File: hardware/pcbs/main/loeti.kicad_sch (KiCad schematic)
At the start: 104 parts, among them J1 REDFIT_SWD_6, J2 DATA, J3 POWER, J5 Conn_01x05_Pin, Q1 Si4162DY, Q2 BC817, Q4 BC817, Q5 BC807, Q6 Si4425FDY, SW1 BOOT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

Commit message: feat: improve code structure, EEPROM with checksum
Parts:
- Q6: value Si4425FDY -> Si4825
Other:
- note added: "Possible candidates Si4825DDY Si4425DDY DMP3036SSS"
- note removed: "Possible candidates Si4425FDY (best) Si4425DDY Si4825DDY DMG4435SSS IRF9393PbF"
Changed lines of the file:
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@@
 		)
 	)
-	(text "Possible candidates\nSi4425FDY (best)\nSi4425DDY\nSi4825DDY\nDMG4435SSS\nIRF9393PbF"
+	(text "Possible candidates\nSi4825DDY\nSi4425DDY\nDMP3036SSS"
 		(exclude_from_sim no)
 		(at 390.144 154.94 0)
@@
 		)
 	)
+	(polyline
+		(pts
+			(xy 402.59 196.85) (xy 403.86 196.85)
+		)
+		(stroke
+			(width 0)
+			(type solid)
+		)
+	)
 	(wire
 		(pts
@@
 		(on_board yes)
 		(dnp no)
-		(fields_autoplaced yes)
 		(property "Reference" "#FLG08"
 			(at 102.235 207.01 0)
@@
 			)
 		)
-		(property "Value" "Si4425FDY"
+		(property "Value" "Si4825"
 			(at 368.3 173.9899 0)
 			(effects

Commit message: fix: pmos type
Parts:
- Q6: value Si4825 -> Si4425FDY
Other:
- note added: "Possible candidates Si4151DY Si4153DY Si4825DDY"
- note removed: "Possible candidates Si4825DDY Si4425DDY DMP3036SSS"
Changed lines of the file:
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@@
 		)
 	)
-	(text "Possible candidates\nSi4825DDY\nSi4425DDY\nDMP3036SSS"
+	(text "Possible candidates\nSi4151DY\nSi4153DY\nSi4825DDY"
 		(exclude_from_sim no)
 		(at 390.144 154.94 0)
@@
 			)
 		)
-		(property "Value" "Si4825"
+		(property "Value" "Si4425FDY"
 			(at 368.3 173.9899 0)
 			(effects

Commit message: feat: v7a initial hardware design
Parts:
- removed C30: ~, Capacitor_SMD:C_0603_1608Metric, symbol Device:C
- removed U11: TLV333DBV, Package_TO_SOT_SMD:SOT-23-5, symbol Amplifier_Operational:TLV2371DBV
- added C2: 100n, Capacitor_SMD:C_0603_1608Metric, symbol Device:C
- added D10: BAT54S, Package_TO_SOT_SMD:SOT-23, symbol Diode:BAT54S
- added R29, R37: 220k, Resistor_SMD:R_0603_1608Metric, symbol Device:R
- added R38: 1k, Resistor_SMD:R_0603_1608Metric, symbol Device:R
- added U7: TLV2333, Package_SO:SOIC-8_3.9x4.9mm_P1.27mm, symbol Amplifier_Operational:TLV2372
- C29: value 330p -> 22p; MPN C1664 -> C1653
- Q6: value Si4425FDY -> Si4825
- R23: value 1M -> 22k; MPN C22935 -> C31850
- R24: value 10k -> 22k; MPN C25804 -> C31850
- R26: value 1k -> 10k; MPN C21190 -> C25804
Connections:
- net +3V3: now also D10.2 (K), U7.8 (V+); no longer R23.1
- net ADC1_IN1: now also D2.3 (COM), R10.2; no longer C29.1, R25.1
- net ADC1_IN2: now also C29.1, R25.2, D10.3 (COM), U7.7; no longer D2.3 (COM), R10.2
- net GND: now also C2.2, D10.1 (A), R29.1, U7.4 (V-)
- net SLP_EXT: now also J5.1 (Pin_1); no longer J5.3 (Pin_3)
- net at C29.2, R26.1: now also R25.1, U7.6 (-); no longer R25.2
- net at R24.2: now also R37.1, U7.2 (-)
- net HEATER renamed RED
- net RED: now also R23.2
- removed net TC+: J5.1 (Pin_1), R23.2, R24.1
- new net: C2.1, R38.2, U7.5 (+)
- new net: R23.1, R29.2, U7.3 (+)
- new net: R37.2, R38.1, U7.1
- new net GREEN: J5.3 (Pin_3), R24.1
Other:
- note added: "Feedback: ~33 kHz low-pass"
- note added: "Gain 10"
- note added: "Gain 23"
- note added: "Possible candidates Si4825DDY Si4425DDY DMP3036SSS"
- note added: "Thermocouple amplifier - gain 230"
- note added: "~1.6 kHz low-pass"
- note removed: "C210 1_COM: green+blue 2_TC+: red 3_HEATER: red"
- note removed: "C245 1_COM: green 2_TC+: red 3_HEATER: blue"
- note removed: "Feedback: 2180 Hz low-pass"
- note removed: "Possible candidates Si4151DY Si4153DY Si4825DDY"
- note removed: "Thermocouple amplifier"
- moved on the sheet: D2, J5, R10, R24, R25, R9

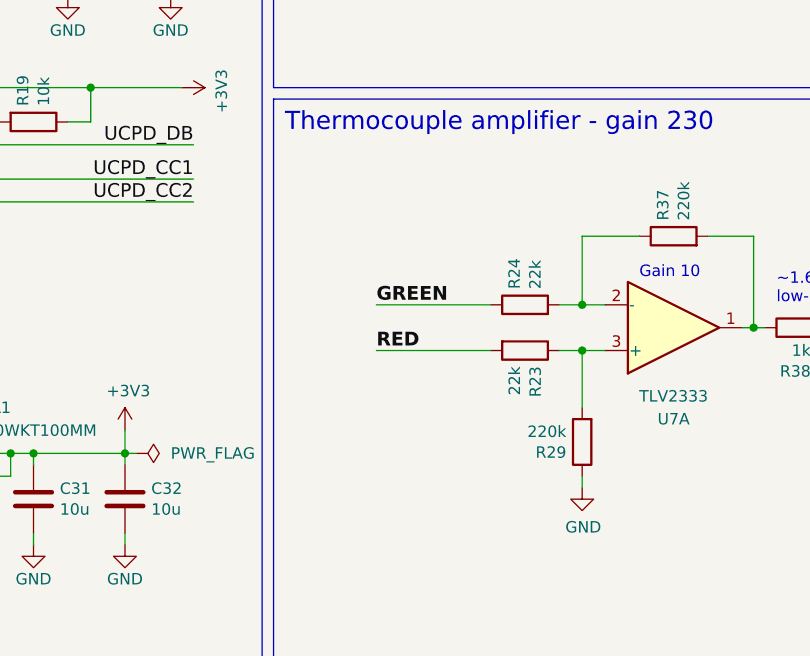
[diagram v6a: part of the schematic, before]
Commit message: feat: support multiple board variants
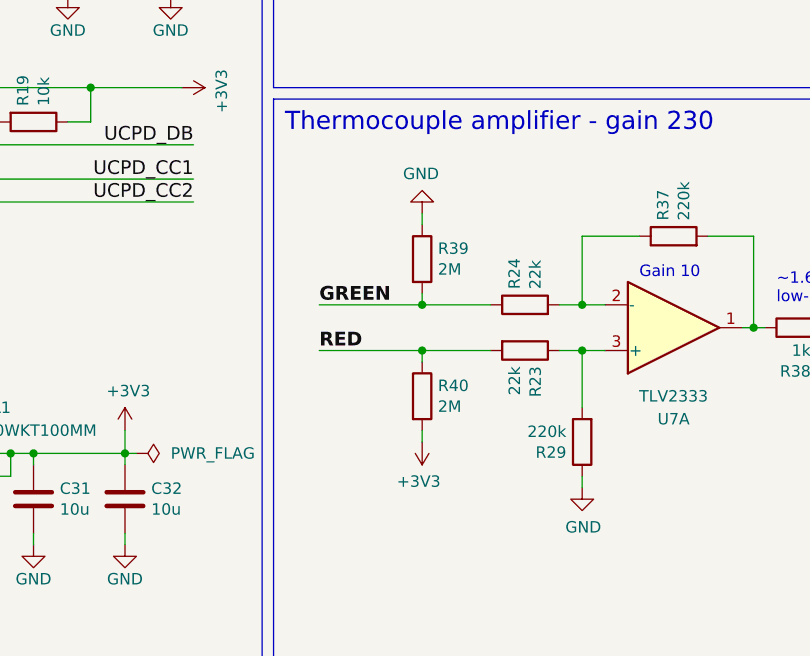
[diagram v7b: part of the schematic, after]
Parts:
- added R39, R40: 2M, Resistor_SMD:R_0603_1608Metric, symbol Device:R
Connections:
- net +3V3: now also R40.2
- net GND: now also R39.1
- net GREEN: now also R39.2
- net RED: now also R40.1

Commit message: feat: hw v7a
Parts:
- U4: symbol MCU_ST_STM32G4:STM32G431CBTx -> MCU_ST_STM32G4:STM32G491CCTx
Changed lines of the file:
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@@
 	)
 	(symbol
-		(lib_id "MCU_ST_STM32G4:STM32G431CBTx")
+		(lib_id "MCU_ST_STM32G4:STM32G491CCTx")
 		(at 200.66 64.77 0)
 		(unit 1)
@@
 		)
 		(property "Footprint" "Package_QFP:LQFP-48_7x7mm_P0.5mm"
-			(at 187.96 100.33 0)
+			(at 185.42 102.87 0)
 			(effects
 				(font
@@
 			)
 		)
-		(property "Datasheet" "https://www.st.com/resource/en/datasheet/stm32g431cb.pdf"
+		(property "Datasheet" "https://www.st.com/resource/en/datasheet/stm32g491cc.pdf"
 			(at 200.66 64.77 0)
 			(effects
@@
 			)
 		)
-		(property "Description" "STMicroelectronics Arm Cortex-M4 MCU, 128KB flash, 32KB RAM, 170 MHz, 1.71-3.6V, 38 GPIO, LQFP48"
+		(property "Description" "STMicroelectronics Arm Cortex-M4 MCU, 256KB flash, 112KB RAM, 170 MHz, 1.71-3.6V, 38 GPIO, LQFP48"
 			(at 200.66 64.77 0)
 			(effects
